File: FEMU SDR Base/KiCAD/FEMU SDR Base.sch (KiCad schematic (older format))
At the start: 69 parts, among them P1 Battery, P10 PWM2, P11 PWM3, P12 PWM4, P13 PWM1, P14 PWM2, P15 PWM3, P16 PWM4, P17 12V, P18 GND, P19 12V, P2 SDR_Shield_1, P20 GND, P21 S0GND, P22 S1GND, P23 S0DN, P24 S1DN, P25 S0DP, P26 S1DP, P27 PWM0, P28 PWM5, P29 PWM6, P3 SDR_Shield_2, P30 PWM7, P31 PWM0, P32 PWM5, P33 PWM6, P34 PWM7, P35 Battery, P4 12V, P5 GND, P6 12V, P7 GND, P8 Raspi_Power_Shield, P9 PWM1, U1 TPS562209, U2 LP38858-LDO, U3 LP38858-LDO, U4 7833, U5 7833

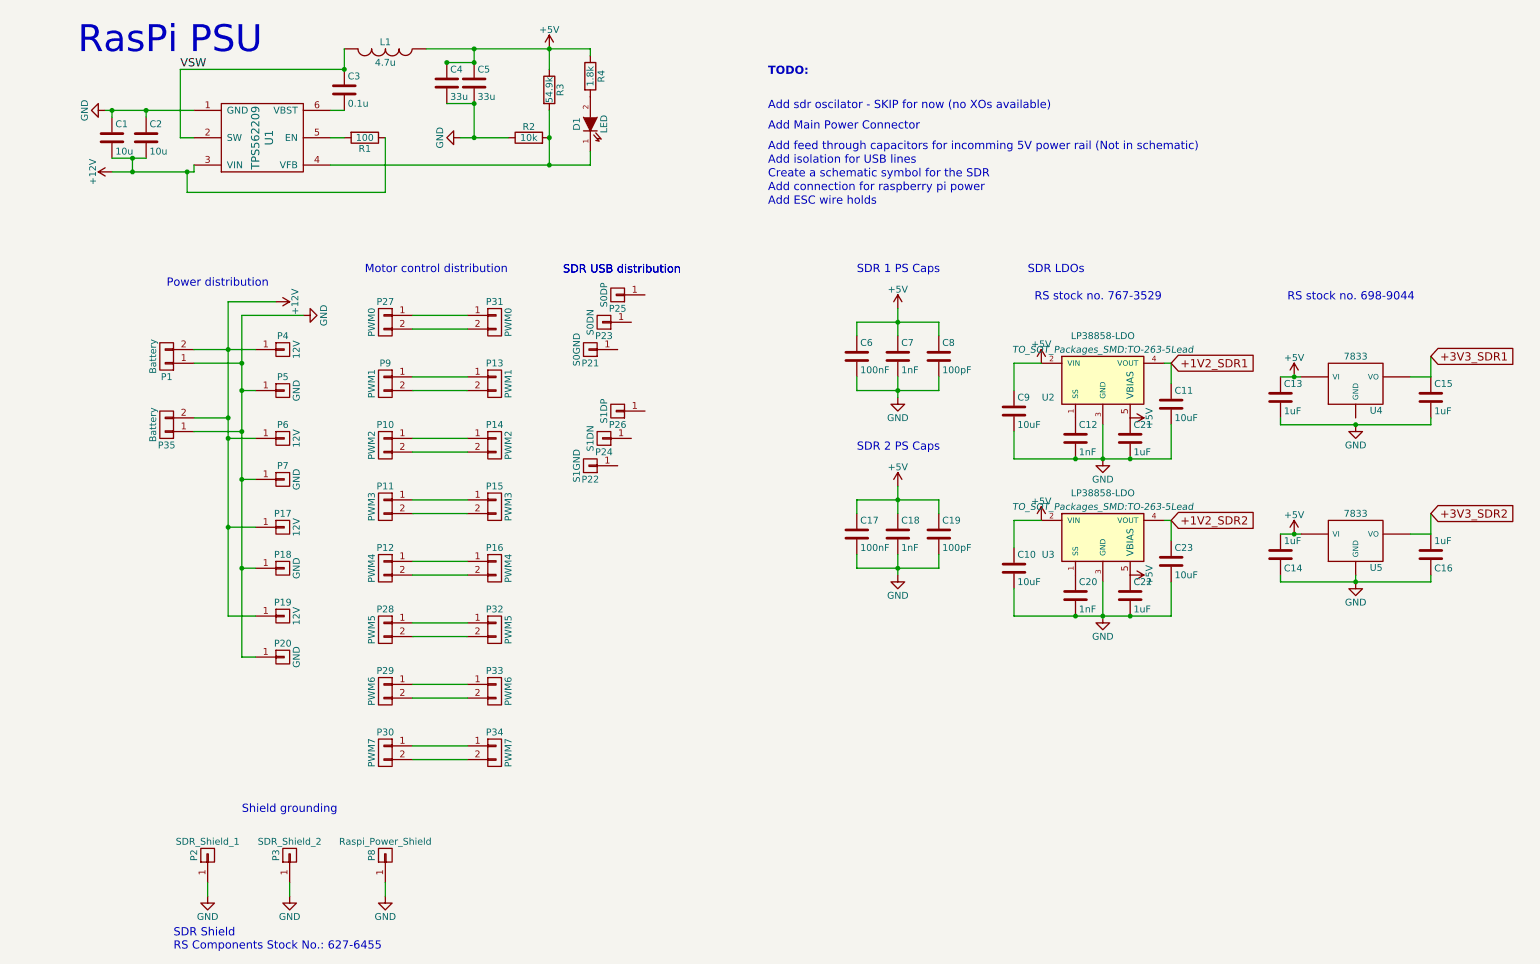
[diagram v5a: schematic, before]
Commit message: Added esc mounts, power headers and usb headers
Signed-off-by: hardiepienaar <hardiepienaar@gmail.com>
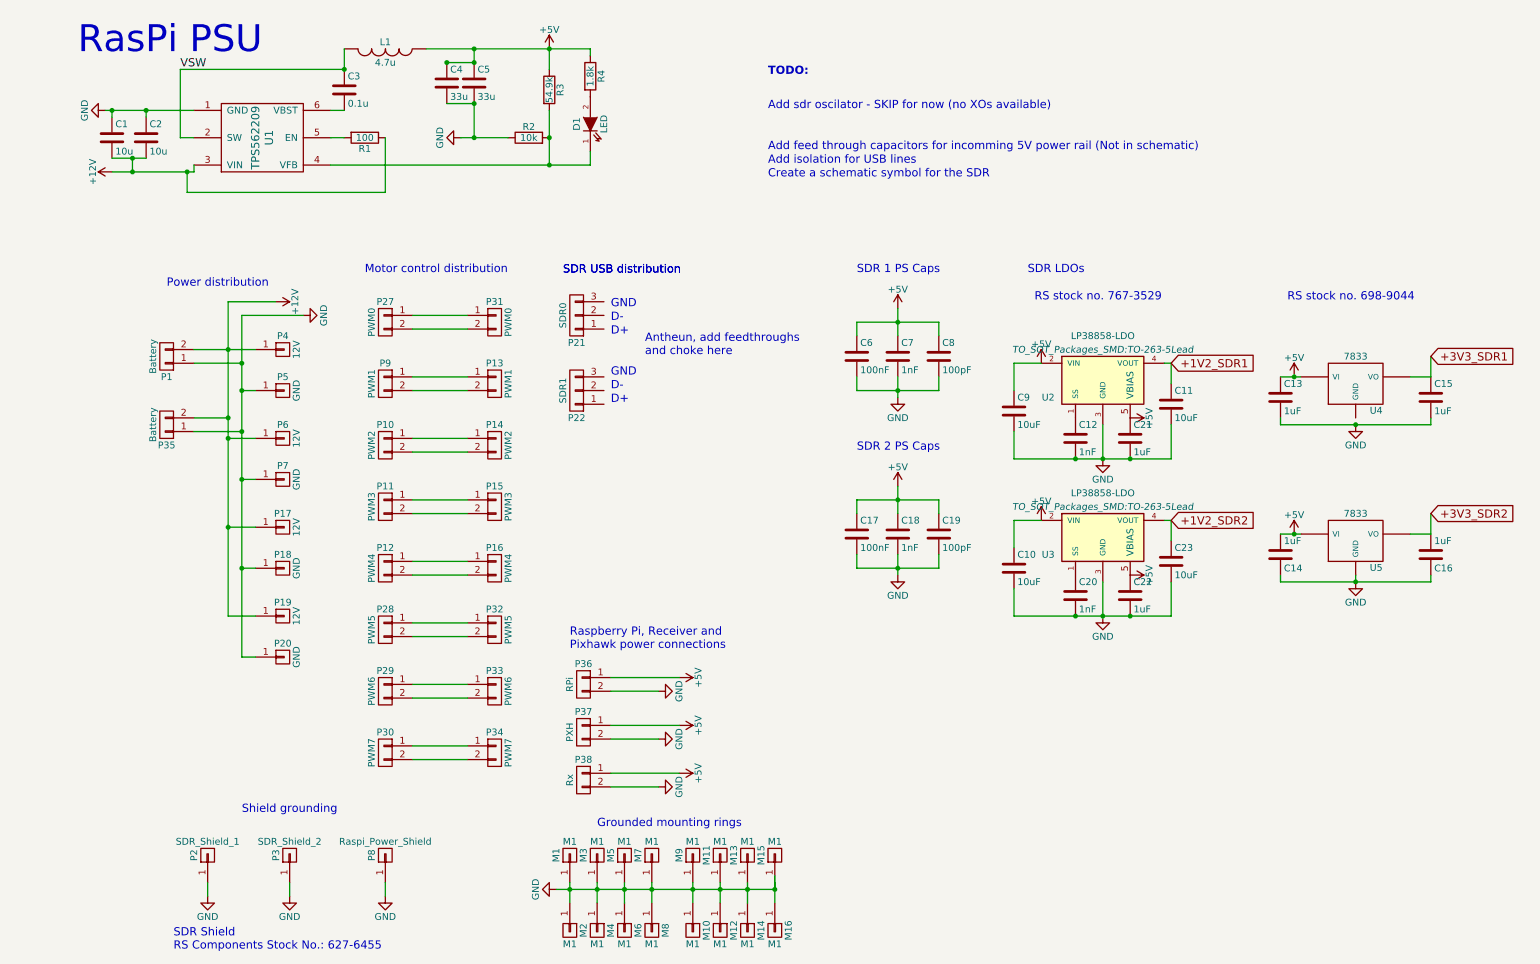
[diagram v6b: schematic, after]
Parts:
- removed P21: S0GND, SMD_Packages:1Pin, symbol CONN_01X01
- removed P22: S1GND, SMD_Packages:1Pin, symbol CONN_01X01
- removed P23: S0DN, SMD_Packages:1Pin, symbol CONN_01X01
- removed P24: S1DN, SMD_Packages:1Pin, symbol CONN_01X01
- removed P25: S0DP, SMD_Packages:1Pin, symbol CONN_01X01
- removed P26: S1DP, SMD_Packages:1Pin, symbol CONN_01X01
- added M1, M10, M11, M12, M13, M14, M15, M16, M2, M3, M4, M5, M6, M7, M8, M9: M1, Misc footprints:MountHole, symbol CONN_01X01
- added P21: SDR0, Misc footprints:USB, symbol CONN_01X03
- added P22: SDR1, Misc footprints:USB, symbol CONN_01X03
- added P36: RPi, SMD_Packages:SMD-1206_Pol, symbol CONN_01X02
- added P37: PXH, SMD_Packages:SMD-1206_Pol, symbol CONN_01X02
- added P38: Rx, SMD_Packages:SMD-1206_Pol, symbol CONN_01X02
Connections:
- net +5V: now also P36.1 (P1), P37.1 (P1), P38.1 (P1)
- net GND: now also M1.1 (P1), M10.1 (P1), M11.1 (P1), M12.1 (P1), M13.1 (P1), M14.1 (P1), M15.1 (P1), M16.1 (P1), M2.1 (P1), M3.1 (P1), M4.1 (P1), M5.1 (P1), M6.1 (P1), M7.1 (P1), M8.1 (P1), M9.1 (P1), P36.2 (P2), P37.2 (P2), P38.2 (P2)
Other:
- note added: "Antheun, add feedthroughs \nand choke here"
- note added: "D+\n"
- note added: "D-\n"
- note added: "GND"
- note added: "Grounded mounting rings\n\n"
- note added: "Raspberry Pi, Receiver and \nPixhawk power connections"
- note removed: "Add ESC wire holds\n"
- note removed: "Add Main Power Connector"
- note removed: "Add connection for raspberry pi power\n"

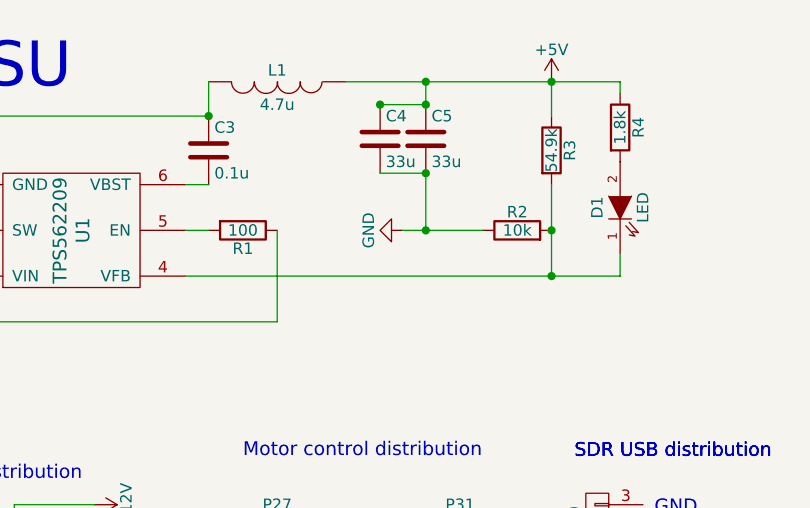
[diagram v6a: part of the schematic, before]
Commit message: Added Stitching to RasPi PSU and finished this layout, added feedthrough and CM filter foots
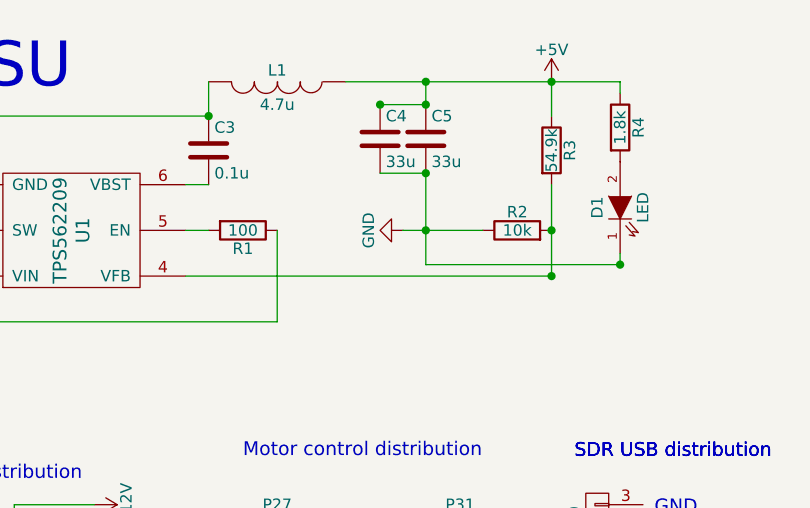
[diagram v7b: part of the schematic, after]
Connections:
- net GND: now also D1.1 (K)
- net at R2.2, R3.2, U1.4 (VFB): no longer D1.1 (K)
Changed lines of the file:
@@
 Wire Wire Line
 	3900 1150 3900 1550
-Wire Wire Line
-	2300 1550 4200 1550
 Connection ~ 3900 1350
 Connection ~ 3350 1100
 Wire Wire Line
-	3350 1100 3350 1350
+	3350 1100 3350 1500
 Wire Wire Line
 	3250 1350 3600 1350
@@
 	4200 700  4200 750
 Connection ~ 3900 1550
-Wire Wire Line
-	4200 1550 4200 1450
 $Comp
 L CONN_01X02 P35
@@
 Text Notes 4350 2600 0    60   ~ 0
 GND
+Wire Wire Line
+	3900 1550 2300 1550
+Wire Wire Line
+	3350 1500 4200 1500
+Connection ~ 4200 1500
+Wire Wire Line
+	4200 1500 4200 1450
 $EndSCHEMATC

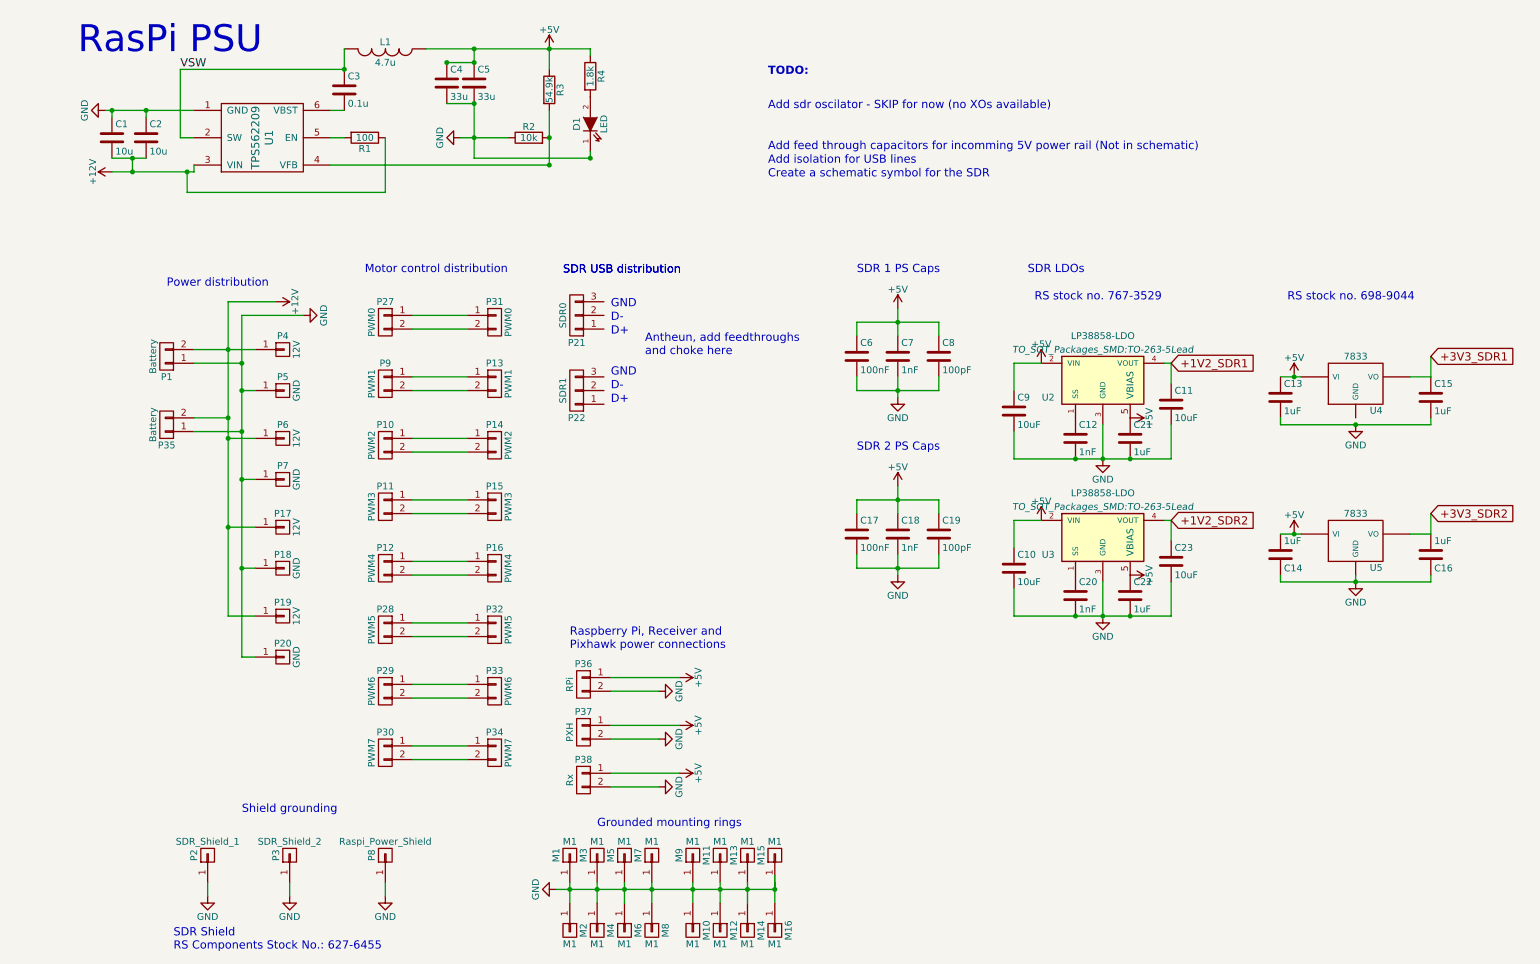
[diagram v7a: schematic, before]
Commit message: STATUS=FREE, SDR1 arranged
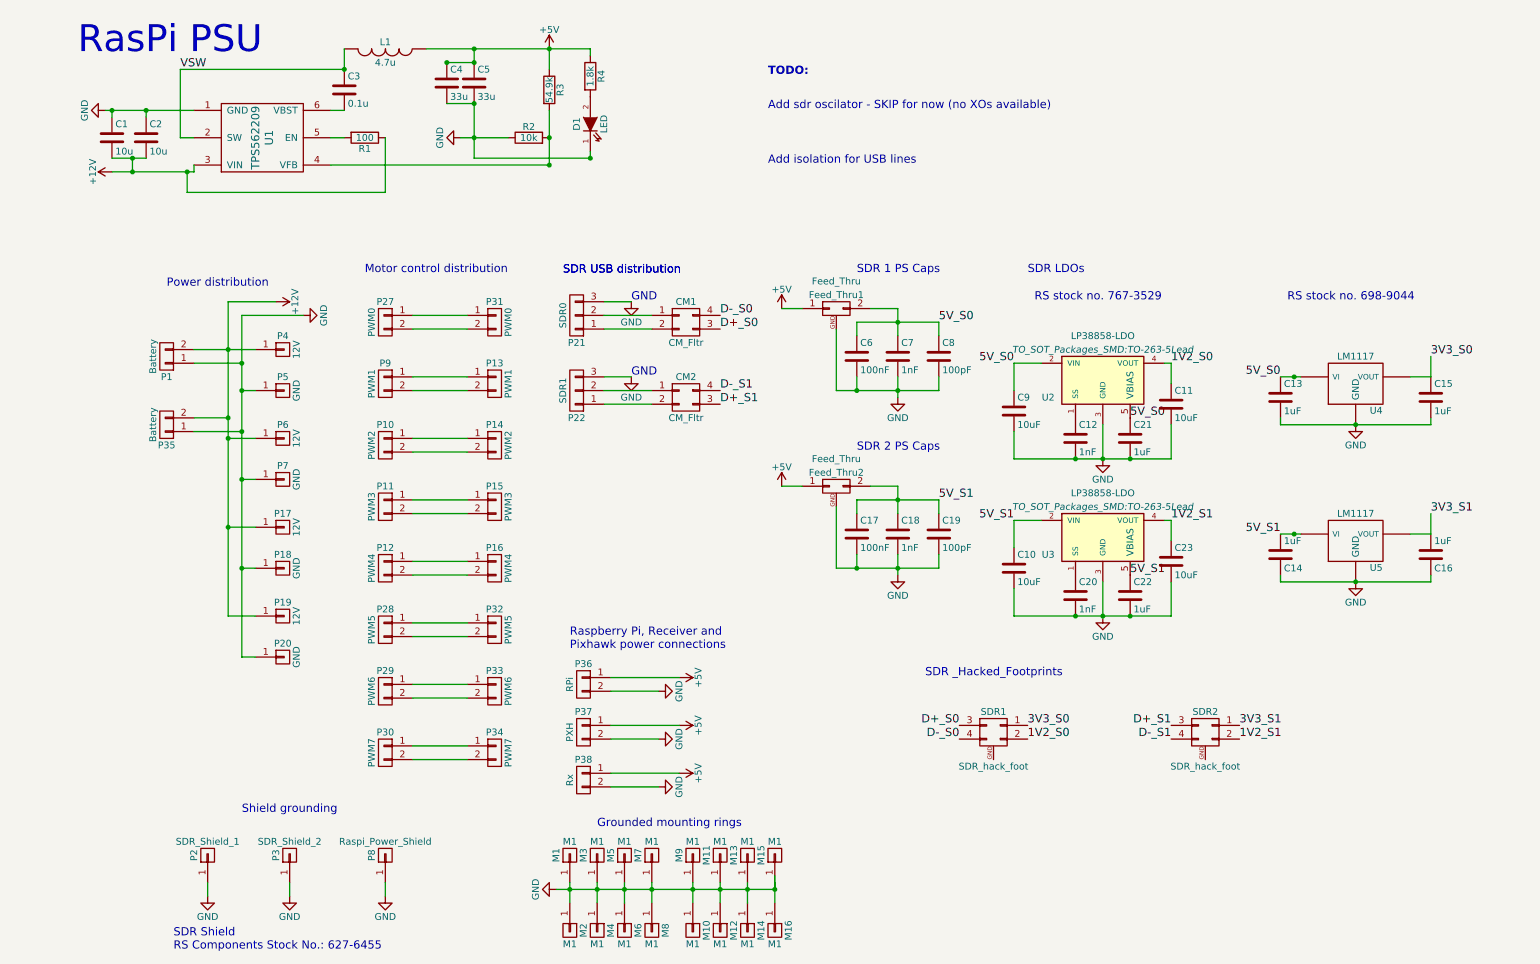
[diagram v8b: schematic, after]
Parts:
- removed U4, U5: 7833, TO_SOT_Packages_SMD:TO-252-2Lead, symbol 7833
- added CM1, CM2: CM_Fltr, ARB_foots:TDK_ACM_CM_filter, symbol CM_Fltr
- added Feed_Thru1, Feed_Thru2: Feed_Thru, ARB_foots:AVX_W#F_FeedThrough_SMD_Caps, symbol Feed_Thru
- added SDR1, SDR2: SDR_hack_foot, ARB_foots:SDR_hack_outline, symbol SDR_hack_foot
- added U4, U5: LM1117, TO_SOT_Packages_SMD:TO-252-2Lead, symbol LM1117
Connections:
- net +5V: now also Feed_Thru1.1 (P1), Feed_Thru2.1 (P1); no longer C10.1, C13.1, C14.2, C17.1, C18.1, C19.1, C21.1, C22.1, C6.1, C7.1, C8.1, C9.1, U2.2 (VIN), U2.5 (VBIAS), U3.2 (VIN), U3.5 (VBIAS)
- net GND: now also P21.3 (P3), P22.3 (P3), Feed_Thru1.GND, Feed_Thru2.GND, U4.2 (GND), U5.2 (GND)
- net at P21.1 (P1): now also CM1.2 (P3)
- net at P21.2 (P2): now also CM1.1 (P1)
- net at P22.1 (P1): now also CM2.2 (P3)
- net at P22.2 (P2): now also CM2.1 (P1)
- net +1V2_SDR1 renamed 1V2_S0
- net 1V2_S0: now also SDR1.2 (P2)
- net +1V2_SDR2 renamed 1V2_S1
- net 1V2_S1: now also SDR2.2 (P2)
- net +3V3_SDR1 renamed 3V3_S0
- net 3V3_S0: now also SDR1.1 (P1), U4.3 (VOUT)
- net +3V3_SDR2 renamed 3V3_S1
- net 3V3_S1: now also SDR2.1 (P1), U5.3 (VOUT)
- new net 5V_S0: C13.1, C21.1, C6.1, C7.1, C8.1, C9.1, Feed_Thru1.2 (P2), U2.2 (VIN), U2.5 (VBIAS), U4.1 (VI)
- new net 5V_S1: C10.1, C14.2, C17.1, C18.1, C19.1, C22.1, Feed_Thru2.2 (P2), U3.2 (VIN), U3.5 (VBIAS), U5.1 (VI)
- new net D+_S0: CM1.3 (P4), SDR1.3 (P3)
- new net D+_S1: CM2.3 (P4), SDR2.3 (P3)
- new net D-_S0: CM1.4 (P2), SDR1.4 (P4)
- new net D-_S1: CM2.4 (P2), SDR2.4 (P4)
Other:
- note added: "SDR _Hacked_Footprints"
- note removed: "Add feed through capacitors for incomming 5V power rail (Not in schematic)"
- note removed: "Antheun, add feedthroughs \nand choke here"
- note removed: "Create a schematic symbol for the SDR"
- note removed: "D+\n"
- note removed: "D-\n"
